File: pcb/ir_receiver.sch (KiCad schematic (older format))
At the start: 6 parts, among them IC8 AD8604

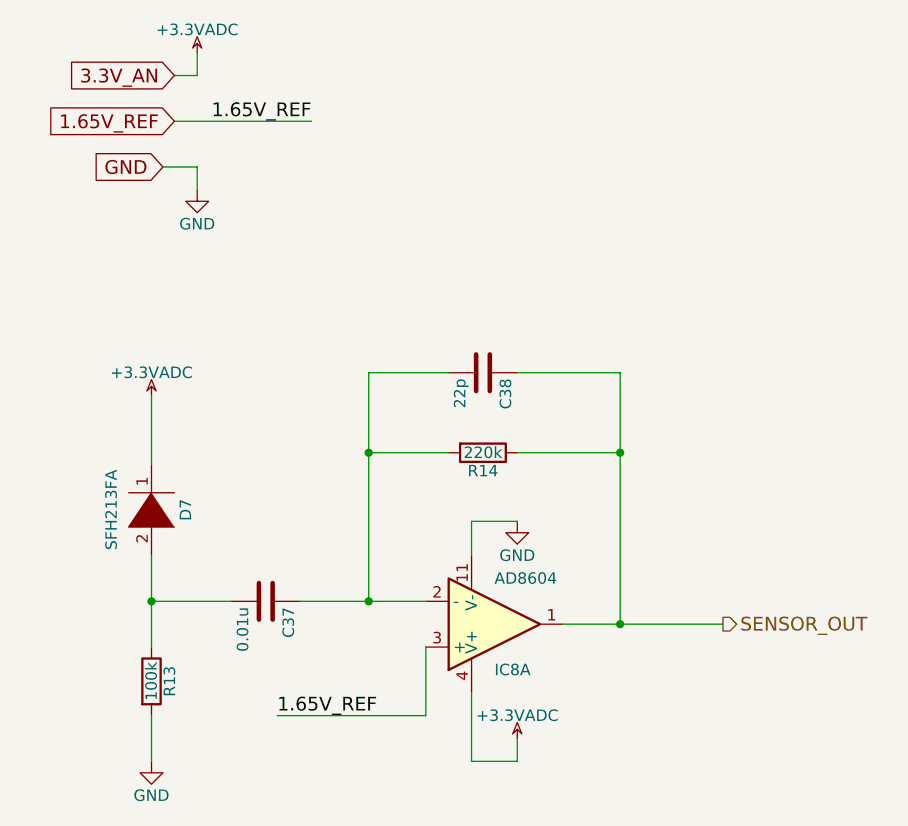
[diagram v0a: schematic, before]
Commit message: 回路図を修正 ・赤外線LEDの発光回路にpull down抵抗を追加 ・赤外線LEDの発光回路の電流制限抵抗の値を変更
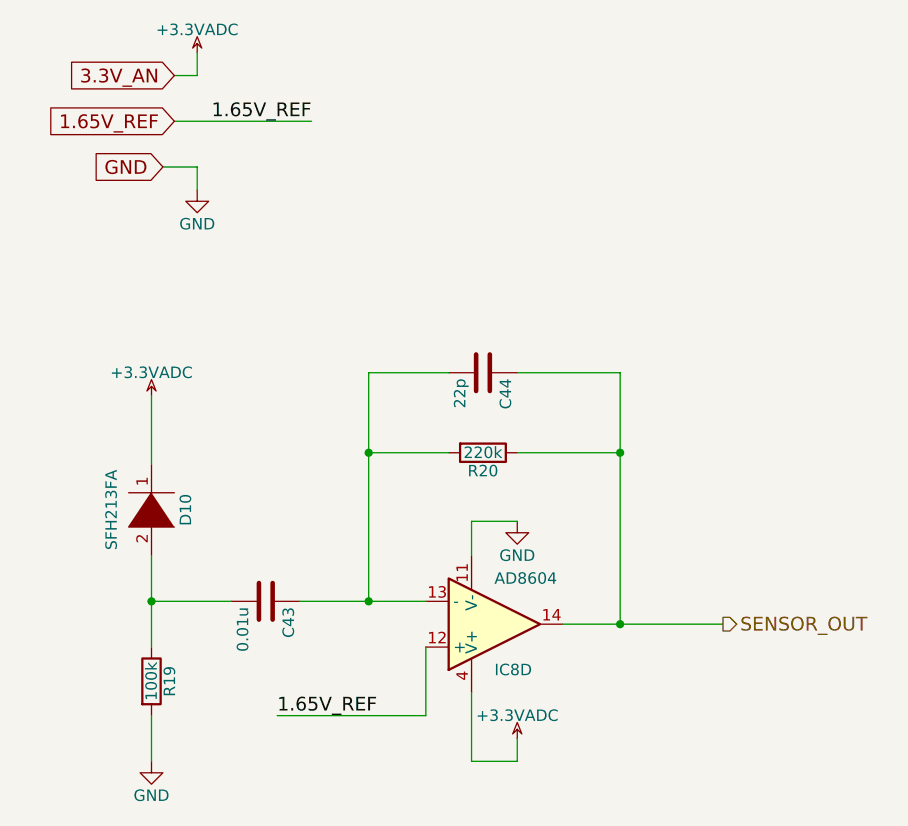
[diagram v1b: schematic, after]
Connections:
- net 1.65V_REF: now also IC8.12 (+); no longer IC8.3 (+)
- net SENSOR_OUT: now also IC8.14; no longer IC8.1
- net at C37.1, C38.2, R14.2: now also IC8.13 (-); no longer IC8.2 (-)
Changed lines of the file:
@@
 $Descr A4 11693 8268
 encoding utf-8
-Sheet 9 12
+Sheet 10 12
 Title ""
 Date ""
@@
 AR Path="/57CD844F/57DF9723" Ref="D9"  Part="1"
 AR Path="/57E4FEED/57DF9723" Ref="D10"  Part="1"
-F 0 "D7" H 4500 4350 50  0000 C CNN
+F 0 "D10" H 4500 4350 50  0000 C CNN
 F 1 "SFH213FA" H 4500 4025 50  0000 C CNN
 F 2 "micromouse2016:LED_5mm_angle" H 4500 4200 50  0001 C CNN
@@
 AR Path="/57CD844F/57DF9784" Ref="R17"  Part="1"
 AR Path="/57E4FEED/57DF9784" Ref="R19"  Part="1"
-F 0 "R13" V 4580 4950 50  0000 C CNN
+F 0 "R19" V 4580 4950 50  0000 C CNN
 F 1 "100k" V 4500 4950 50  0000 C CNN
 F 2 "Resistors_SMD:R_0603" V 4430 4950 50  0001 C CNN
@@
 AR Path="/57CD844F/57DF980D" Ref="C41"  Part="1"
 AR Path="/57E4FEED/57DF980D" Ref="C43"  Part="1"
-F 0 "C37" H 5025 4700 50  0000 L CNN
+F 0 "C43" H 5025 4700 50  0000 L CNN
 F 1 "0.01u" H 5025 4500 50  0000 L CNN
 F 2 "Capacitors_SMD:C_0603" H 5038 4450 50  0001 C CNN
@@
 $Comp
 L AD8604 IC8
-U 1 1 57DF986C
+U 4 1 57DF986C
 P 6000 4700
 AR Path="/57E4FC7A/57DF986C" Ref="IC8"  Part="1"
@@
 F 2 "Housings_SSOP:TSSOP-14_4.4x5mm_Pitch0.65mm" H 5950 4800 50  0001 C CNN
 F 3 "" H 6050 4900 50  0000 C CNN
-	1    6000 4700
+	4    6000 4700
 	1    0    0    1
 $EndComp
@@
 AR Path="/57CD844F/57DF98CC" Ref="R18"  Part="1"
 AR Path="/57E4FEED/57DF98CC" Ref="R20"  Part="1"
-F 0 "R14" V 6030 3950 50  0000 C CNN
+F 0 "R20" V 6030 3950 50  0000 C CNN
 F 1 "220k" V 5950 3950 50  0000 C CNN
 F 2 "Resistors_SMD:R_0603" V 5880 3950 50  0001 C CNN
@@
 AR Path="/57CD844F/57DF990F" Ref="C42"  Part="1"
 AR Path="/57E4FEED/57DF990F" Ref="C44"  Part="1"
-F 0 "C38" H 5975 3700 50  0000 L CNN
+F 0 "C44" H 5975 3700 50  0000 L CNN
 F 1 "22p" H 5975 3500 50  0000 L CNN
 F 2 "Capacitors_SMD:C_0603" H 5988 3450 50  0001 C CNN
@@
 AR Path="/57CD844F/57DF9947" Ref="#PWR0104"  Part="1"
 AR Path="/57E4FEED/57DF9947" Ref="#PWR0110"  Part="1"
-F 0 "#PWR092" H 4500 5050 50  0001 C CNN
+F 0 "#PWR0110" H 4500 5050 50  0001 C CNN
 F 1 "GND" H 4500 5150 50  0000 C CNN
 F 2 "" H 4500 5300 50  0000 C CNN
@@
 AR Path="/57CD844F/57DF9973" Ref="#PWR0105"  Part="1"
 AR Path="/57E4FEED/57DF9973" Ref="#PWR0111"  Part="1"
-F 0 "#PWR093" H 6100 4000 50  0001 C CNN
+F 0 "#PWR0111" H 6100 4000 50  0001 C CNN
 F 1 "GND" H 6100 4100 50  0000 C CNN
 F 2 "" H 6100 4250 50  0000 C CNN
@@
 AR Path="/57CD844F/57DF999F" Ref="#PWR0106"  Part="1"
 AR Path="/57E4FEED/57DF999F" Ref="#PWR0112"  Part="1"
-F 0 "#PWR094" H 6250 5150 50  0001 C CNN
+F 0 "#PWR0112" H 6250 5150 50  0001 C CNN
 F 1 "+3.3VADC" H 6100 5300 50  0000 C CNN
 F 2 "" H 6100 5200 50  0000 C CNN
@@
 AR Path="/57CD844F/57DF99CB" Ref="#PWR0107"  Part="1"
 AR Path="/57E4FEED/57DF99CB" Ref="#PWR0113"  Part="1"
-F 0 "#PWR095" H 4650 3650 50  0001 C CNN
+F 0 "#PWR0113" H 4650 3650 50  0001 C CNN
 F 1 "+3.3VADC" H 4500 3800 50  0000 C CNN
 F 2 "" H 4500 3700 50  0000 C CNN
@@
 AR Path="/57CD844F/57DF9DAB" Ref="#PWR0108"  Part="1"
 AR Path="/57E4FEED/57DF9DAB" Ref="#PWR0114"  Part="1"
-F 0 "#PWR096" H 4850 2150 50  0001 C CNN
+F 0 "#PWR0114" H 4850 2150 50  0001 C CNN
 F 1 "+3.3VADC" H 4700 2300 50  0000 C CNN
 F 2 "" H 4700 2200 50  0000 C CNN
@@
 AR Path="/57CD844F/57DF9E1D" Ref="#PWR0109"  Part="1"
 AR Path="/57E4FEED/57DF9E1D" Ref="#PWR0115"  Part="1"
-F 0 "#PWR097" H 4700 2550 50  0001 C CNN
+F 0 "#PWR0115" H 4700 2550 50  0001 C CNN
 F 1 "GND" H 4700 2650 50  0000 C CNN
 F 2 "" H 4700 2800 50  0000 C CNN
